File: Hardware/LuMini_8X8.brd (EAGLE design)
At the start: 40.6 x 25.4 mm, 110 parts, among them J1 LED_PAD, J10 LED_PAD, J11 LED_PAD, J12 LED_PAD, J13 LED_PAD, J14 LED_PAD, J15 LED_PAD, J16 LED_PAD, J2 LED_PAD, J3 LED_PAD, J4 LED_PAD, J5 LED_PAD, J6 LED_PAD, J7 LED_PAD, J8 LED_PAD, J9 LED_PAD

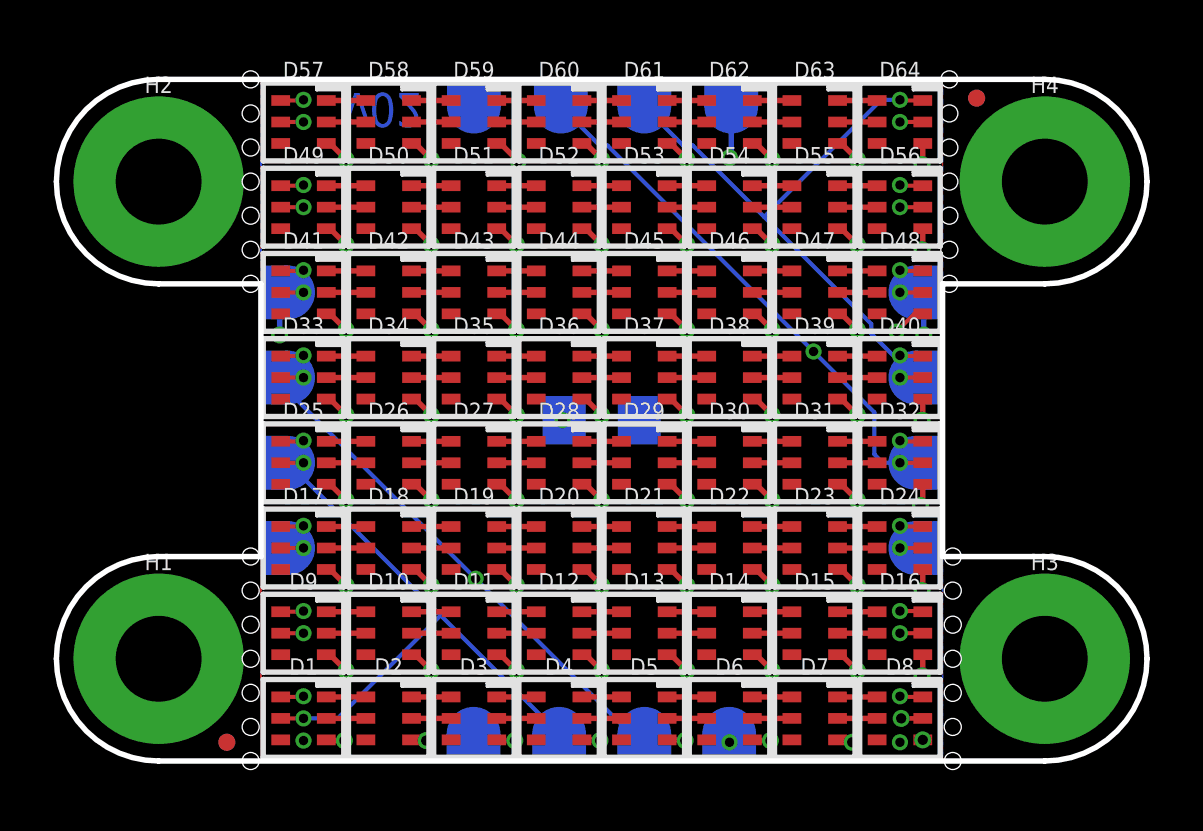
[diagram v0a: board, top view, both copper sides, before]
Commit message: updating to proper footprint
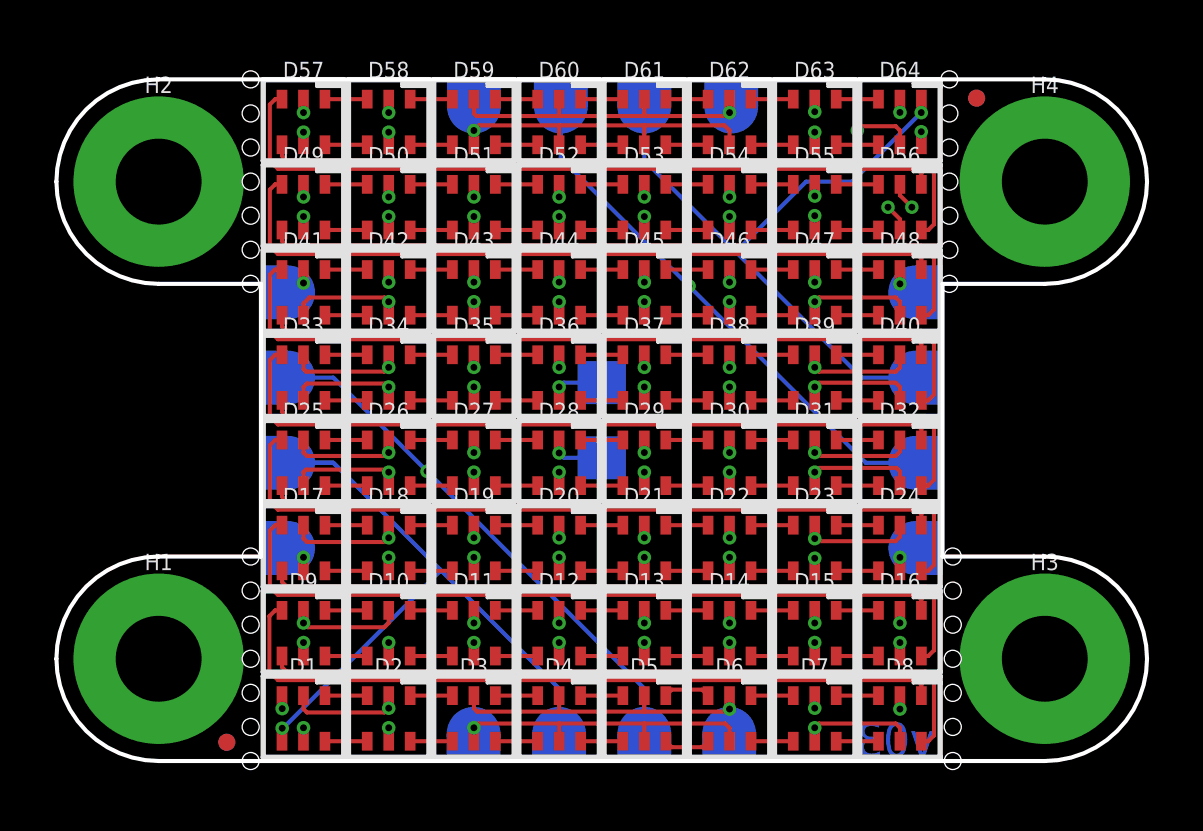
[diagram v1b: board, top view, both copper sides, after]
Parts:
- D1, D10, D11, D12, D13, D14, D15, D16, D17, D18, D19, D2, D20, D21, D22, D23, D24, D25, D26, D27, D28, D29, D3, D30, D31, D32, D33, D34, D35, D36, D37, D38, D39, D4, D40, D41, D42, D43, D44, D45, D46, D47, D48, D49, D5, D50, D51, D52, D53, D54, D55, D56, D57, D58, D59, D6, D60, D61, D62, D63, D64, D7, D8, D9: value APA1022020 -> APA102-2020
- turned C1 to 270 degrees
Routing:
- net GND: track 7.64 -> 83.9 mm, vias 7 -> 50
- net 5V: track 60.5 -> 84.3 mm, vias 64 -> 51
- net CI: track 22.8 -> 28.2 mm
- net DI: track 29.4 -> 33.9 mm
- net DO: track 23.2 -> 26.0 mm
- net N$62: track 26.0 -> 27.5 mm, vias 2 -> 0
- net N$48: track 26.0 -> 27.5 mm, vias 2 -> 0
- net N$34: track 26.0 -> 27.5 mm, vias 2 -> 0
- net N$18: track 26.0 -> 27.5 mm, vias 2 -> 0
- net N$104: track 26.0 -> 27.4 mm, vias 2 -> 0
- net N$90: track 26.0 -> 27.4 mm, vias 2 -> 0
- net N$76: track 26.0 -> 27.4 mm, vias 2 -> 0
- net N$17: track 26.3 -> 27.5 mm, vias 2 -> 0
- net N$61: track 26.3 -> 27.5 mm, vias 2 -> 0
- net N$75: track 26.3 -> 27.5 mm, vias 2 -> 0
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- added copper zone on layer 15, net 5V
- added copper zone on layer 2, net GND
- removed copper zone on layer 16, net 5V
- removed copper zone on layer 2, net 5V
- removed copper zone on layer 1, net GND
- removed copper zone on layer 15, net GND
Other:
- board text added: "v03"
- board text removed: "v02"

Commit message: updating to new silk footprint for additional clarity
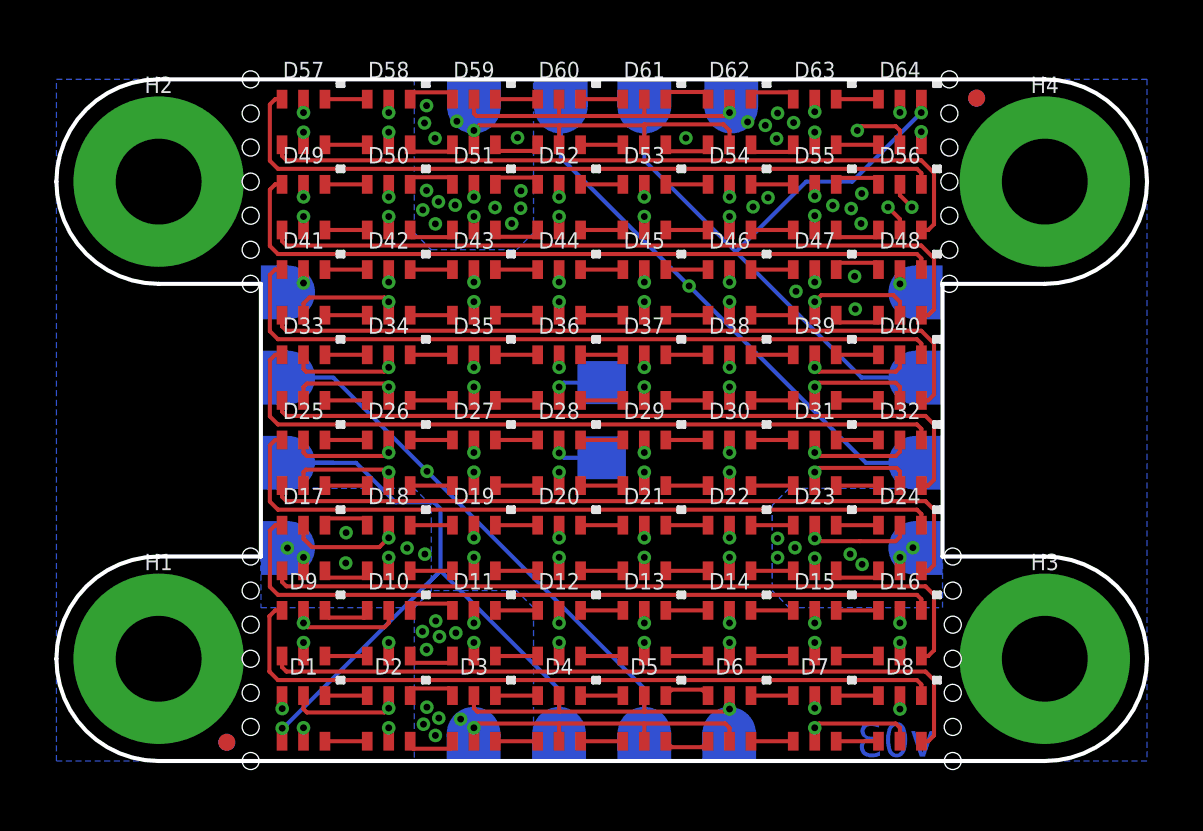
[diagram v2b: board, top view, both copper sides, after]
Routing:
- net CI: track 28.2 -> 29.0 mm
- net N$116: track 1.57 -> 2.09 mm
- net N$94: track 1.58 -> 2.08 mm
- net GND: track 83.9 -> 84.1 mm, vias 50 -> 65
- net 5V: vias 51 -> 86
- added copper zone on layer 16, net 5V
- added copper zone on layer 2, net 5V
- added copper zone on layer 15, net GND
- added copper zone on layer 16, net GND
- removed copper zone on layer 15, net 5V
- removed copper zone on layer 2, net GND

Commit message: removing problem vias
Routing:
- net GND: vias 65 -> 62
- net 5V: vias 86 -> 85
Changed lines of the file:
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@@
 <via x="29.7688" y="16.8402" extent="1-16" drill="0.254"/>
 <via x="27.559" y="17.5006" extent="1-16" drill="0.254"/>
-<via x="30.0101" y="21.1455" extent="1-16" drill="0.254"/>
-<via x="28.9306" y="20.701" extent="1-16" drill="0.254"/>
 <via x="29.9847" y="20.0279" extent="1-16" drill="0.254"/>
-<via x="29.6164" y="20.5867" extent="1-16" drill="0.254"/>
 <via x="25.9588" y="20.6502" extent="1-16" drill="0.254"/>
 <via x="26.5176" y="20.9931" extent="1-16" drill="0.254"/>
@@
 <via x="13.6525" y="20.5359" extent="1-16" drill="0.254"/>
 <via x="14.1224" y="20.0152" extent="1-16" drill="0.254"/>
-<via x="13.0683" y="7.9375" extent="1-16" drill="0.254"/>
 <via x="13.7287" y="7.7089" extent="1-16" drill="0.254"/>
 <wire x1="21.9075" y1="22.9625" x2="21.9075" y2="23.6855" width="0.1524" layer="1"/>

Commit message: updating copper to v10
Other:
- board text added: "v10"
- board text removed: "v03"
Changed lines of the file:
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@@
 <text x="7.62" y="-27.94" size="2.54" layer="51" font="vector">Black PCB
 4 layer board</text>
-<text x="32.73425" y="0.15875" size="1.27" layer="16" font="vector" ratio="15" rot="SMR0">v03</text>
+<text x="32.73425" y="0.15875" size="1.27" layer="16" font="vector" ratio="15" rot="SMR0">v10</text>
 <dimension x1="3.81" y1="21.59" x2="36.83" y2="21.59" x3="20.32" y3="29.21" textsize="1.27" textratio="15" layer="47" unit="inch"/>
 <dimension x1="0" y1="21.59" x2="40.64" y2="21.59" x3="20.32" y3="31.75" textsize="1.27" textratio="15" layer="47" unit="inch"/>
